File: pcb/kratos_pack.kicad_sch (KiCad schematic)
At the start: 96 parts, among them J1 USB_C_Receptacle_USB2.0, J2 PROG_CONN, J3 DBG_UART, J4 BAT_MID+NTC, J5 BAT_7.4V, J6 BAT_0V, J7 OUT+, J8 OUT-, Q1 AON7403, Q2 AON7414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

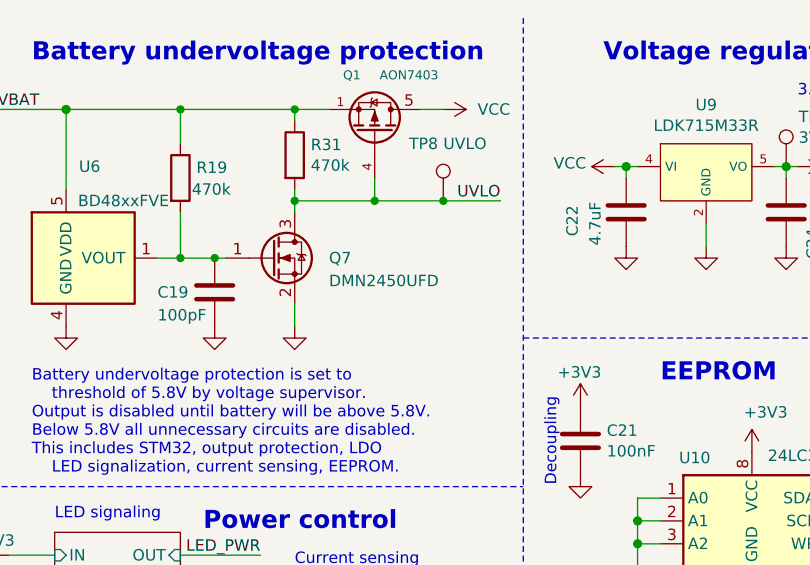
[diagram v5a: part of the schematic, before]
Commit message: Schema: fix incorrect MOSFET model in UVLO invertor
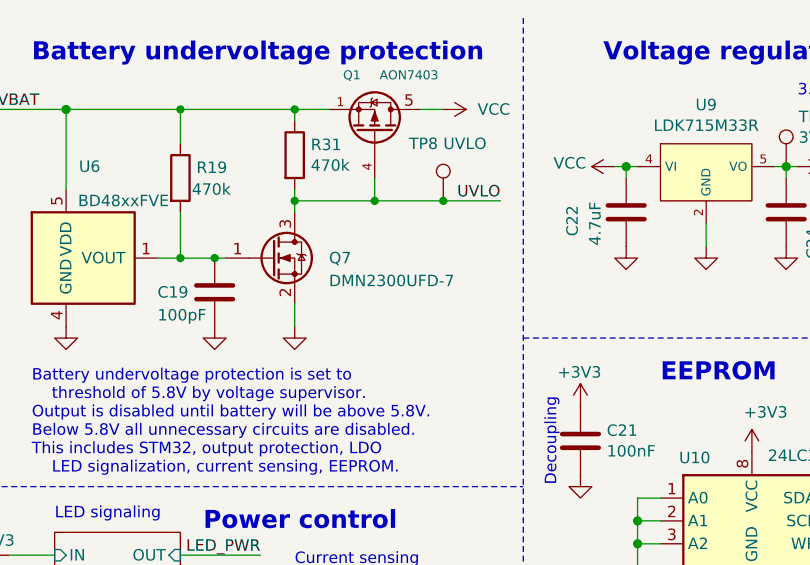
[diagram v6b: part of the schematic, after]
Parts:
- Q7: value DMN2450UFD -> DMN2300UFD-7
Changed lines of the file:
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@@
       (effects (font (size 1.27 1.27)) (justify left))
     )
-    (property "Value" "DMN2450UFD" (id 1) (at 219.71 41.91 0)
+    (property "Value" "DMN2300UFD-7" (id 1) (at 219.71 41.91 0)
       (effects (font (size 1.27 1.27)) (justify left))
     )
@@
     )
     (path "/d9d4b6b8-0fc6-408e-943f-e51fc7c2df5d"
-      (reference "Q7") (unit 1) (value "DMN2450UFD") (footprint "TCY_IC:DFN-3_1.2x1.2mm")
+      (reference "Q7") (unit 1) (value "DMN2300UFD-7") (footprint "TCY_IC:DFN-3_1.2x1.2mm")
     )
     (path "/682b29b3-72b1-4399-a60c-d33327e4df10"

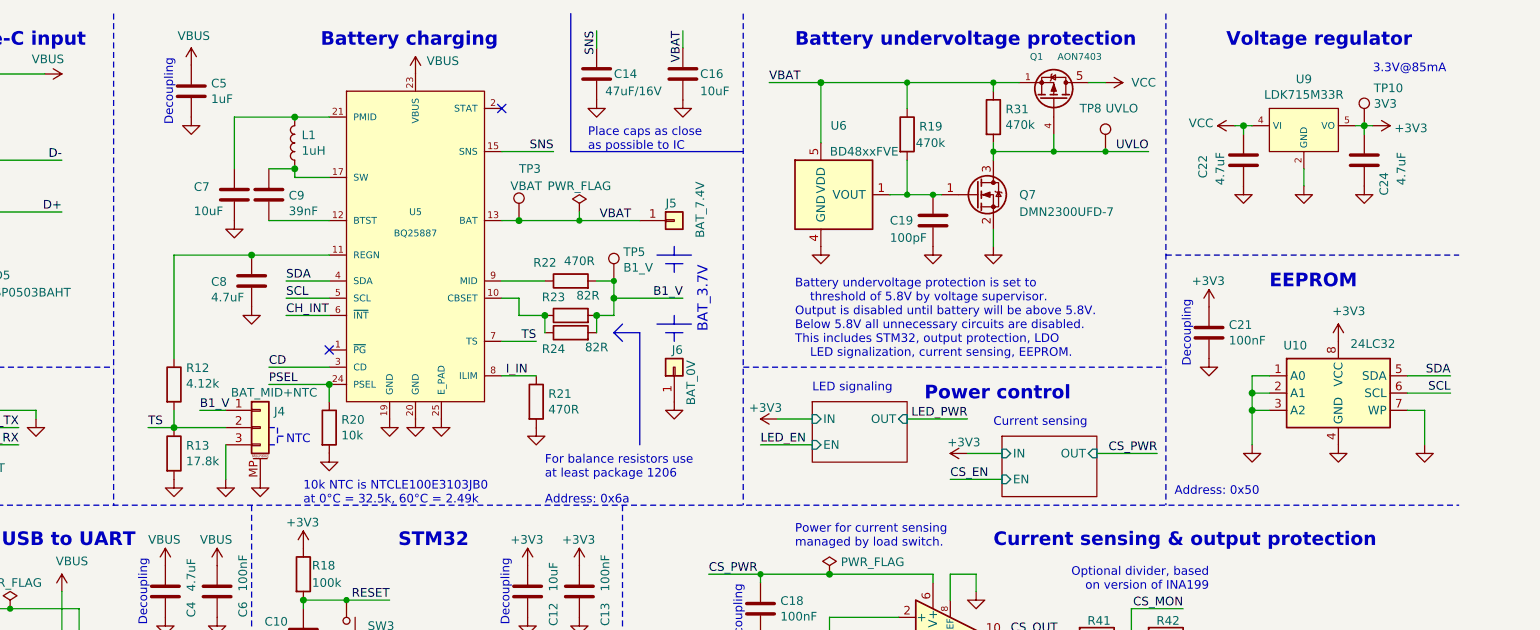
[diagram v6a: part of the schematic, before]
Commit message: Schema & PCB: add jumper selector for 3V3 rail regulator supply (VCC/SNS)
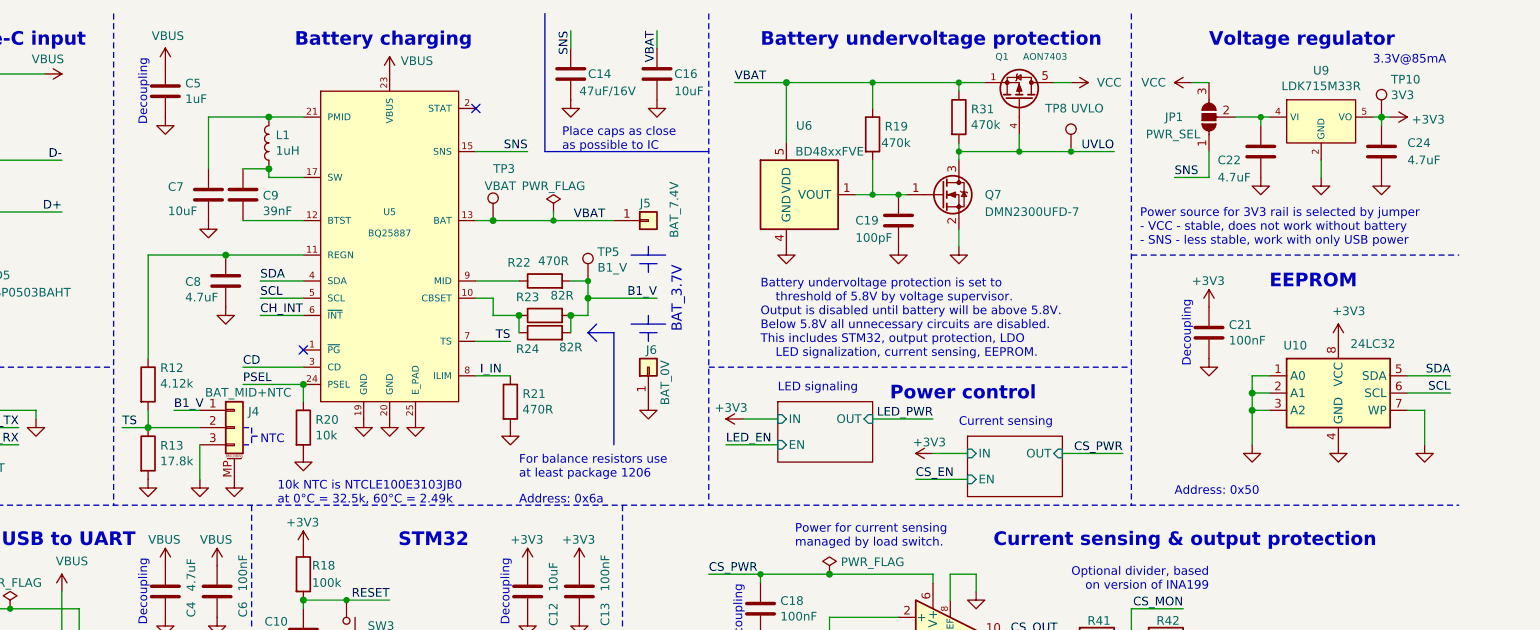
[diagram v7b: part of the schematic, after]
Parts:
- added JP1: PWR_SEL, TCY_connectors:SolderJumper-3_P0.75mm_Open_Pad0.5x0.8mm, symbol Jumper:SolderJumper_3_Open
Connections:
- net SNS: now also JP1.1 (A)
- net VCC: now also JP1.3 (B); no longer C22.1, U9.4 (VI)
- new net: C22.1, JP1.2 (C), U9.4 (VI)
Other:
- note added: "Power source for 3V3 rail is selected by jumper - VCC - stable, does not work without battery - SNS - less stable, work with only USB power"
- moved on the sheet: C14, C16, C19, C22, C24, C5, C7, C8, C9, J4, J5, J6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
